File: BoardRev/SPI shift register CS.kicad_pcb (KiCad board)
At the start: 2 copper layers, 114.3 x 29.2 mm, 22 parts, among them J1 CONN_06, J10 CONN_07, J2 CONN_06, J3 CONN_06, J4 CONN_06, J5 CONN_06, J6 CONN_06, J7 CONN_06, J8 CONN_06, J9 CONN_07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

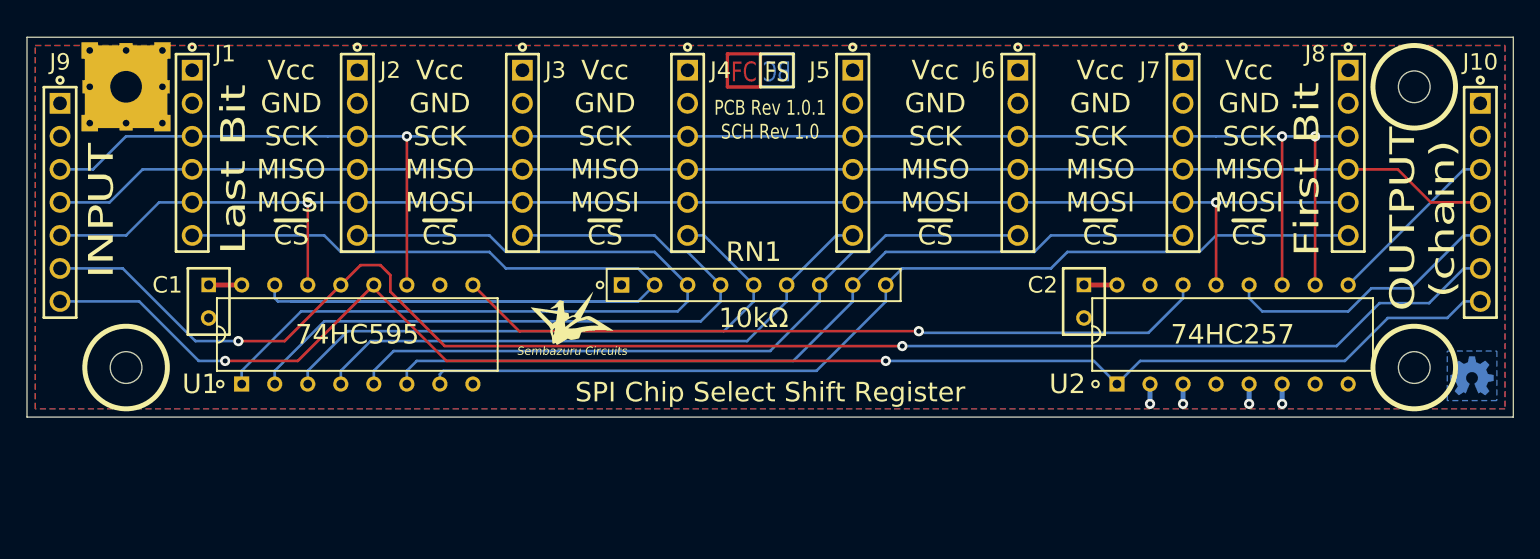
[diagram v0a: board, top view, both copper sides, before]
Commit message: Initial 1" square SMT version
Signed-off-by: Chris 'Sembazuru' Elliott <SembazuruCDE@GMail.com>
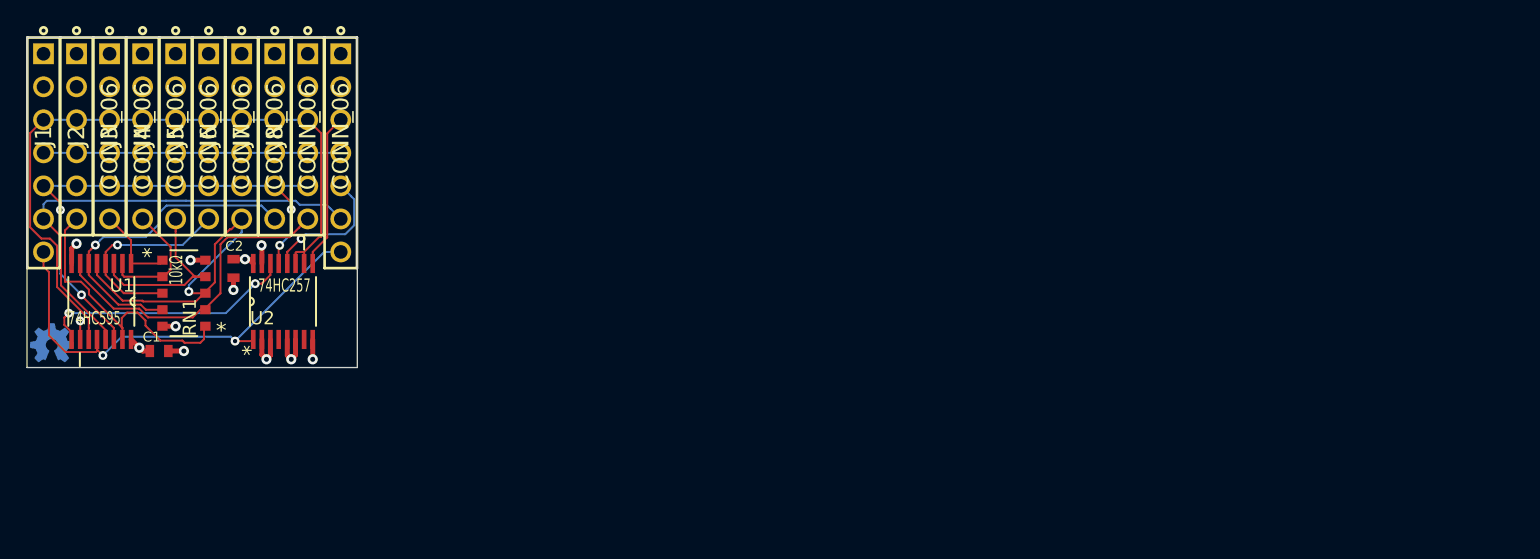
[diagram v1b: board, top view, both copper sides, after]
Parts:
- removed LayerIcon02: VAL**, Misc Unsorted New:LayerIcon02
- removed MH1: #2 Free Fit, ipc-7251TH Standard:MTGP635H244V8P
- removed MH2, MH3, MH4: #2 Free Fit, ipc-7251TH Standard:MTGNP635H244Z635P
- C1, C2: footprint ipc-7251TH Standard:CAPRR254W51L508T318H660P -> AVX-06035C104KAT2A:CAPC1608X90N
- G***: moved to B.Cu
- J1, J2, J3, J4, J5, J6, J7, J8: footprint ipc-7251TH Standard:HDRV6W64P254_1X6_1524X254X1016P -> ipc-7251TH-standard:HDRV6W64P254_1X6_1524X254X1016P
- RN1: footprint ipc-7251TH Standard:SIP249W55P254L2261H495Q9C -> CDE_misc:RESCAV_EXBA-10N
- U1: footprint ipc-7251TH Standard:DIP762W52P254L2159H381Q16C -> NXP-74HC595PW_118:SOP65P640X110-16N
- U2: footprint ipc-7251TH Standard:DIP762W52P254L2159H381Q16C -> TI-SN74HC257PW:SOP65P640X120-16N
- moved G*** 109.2 mm to (78.1, 99.7)
- moved J10 87.7 mm to (100.3, 85.1)
- moved J8 80.0 mm to (97.8, 83.8)
- moved U2 73.1 mm to (95.9, 96.5)
- moved J7 69.9 mm to (95.2, 83.8)
- moved C2 65.5 mm to (92.1, 94.0)
- moved J6 59.7 mm to (92.7, 83.8)
- moved J5 49.5 mm to (90.2, 83.8)
- moved RN1 43.8 mm to (88.3, 95.9), turned to 180 degrees
- moved J4 39.4 mm to (87.6, 83.8)
- moved J3 29.2 mm to (85.1, 83.8)
- moved G*** 21.6 mm to (96.5, 98.4), turned to 180 degrees
- moved U1 19.8 mm to (81.9, 96.5), turned to 270 degrees
- moved J2 19.1 mm to (82.5, 83.8)
- moved J1 8.98 mm to (80.0, 83.8)
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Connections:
- RN1 pad 1: VCC -> /~CS1
- RN1 pad 2: /~CS1 -> /~CS8
- RN1 pad 3: /~CS2 -> /~CS6
- RN1 pad 4: /~CS3 -> /~CS4
- RN1 pad 5: /~CS4 -> VCC
- RN1 pad 6: /~CS5 -> /~CS2
- RN1 pad 7: /~CS6 -> /~CS3
- RN1 pad 8: /~CS7 -> /~CS5
- RN1 pad 9: /~CS8 -> /~CS7
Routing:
- net /MISO: track 111.3 -> 22.9 mm
- net /~dCS: track 119.7 -> 35.9 mm, vias 2 -> 0
- net /~rCS: track 119.5 -> 36.5 mm
- net /SCK: track 134.4 -> 53.5 mm, vias 3 -> 0
- net /~CS1: track 94.7 -> 21.8 mm
- net /MOSI: track 112.8 -> 41.3 mm, vias 2 -> 4
- net /~CS2: track 65.8 -> 6.73 mm
- net /~CS8: track 75.8 -> 25.1 mm
- net /~CS3: track 55.6 -> 9.67 mm
- net /~CS7: track 65.8 -> 25.4 mm, vias 0 -> 1
- net /SerChain: track 58.3 -> 20.0 mm, vias 1 -> 2
- net /~CS4: track 45.4 -> 14.2 mm
- net /~CS6: track 55.6 -> 25.7 mm, vias 0 -> 1
- net /~CS5: track 45.4 -> 15.8 mm, vias 0 -> 1
- net /MOSI/Ser: track 21.6 -> 10.3 mm, vias 0 -> 1
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- added copper zone on In1.Cu, net GND
- added copper zone on In2.Cu, net VCC
- removed copper zone on F.Cu, net GND
- removed copper zone on B.Cu, net VCC
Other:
- board size 114.3 x 29.2 mm -> 25.4 x 25.4 mm
- copper layers 2 -> 4
- net class Default: clearance 0.2032 -> 0.1524; trace_width 0.2032 -> 0.1524; via_dia 0.7874 -> 0.6858; via_drill 0.381 -> 0.3302
- net class Power1A: clearance 0.254 -> 0.1524
- net class Power2A: clearance 0.254 -> 0.1524
- net class Power3A: clearance 0.254 -> 0.1524
- net class Power4A: clearance 0.254 -> 0.1524
- net class Power5A: clearance 0.254 -> 0.1524
- rule trace_clearance: 0.2032 -> 0.1524
- rule trace_min: 0.2032 -> 0.1524
- rule via_min_drill: 0.381 -> 0.3302
- rule via_min_size: 0.7874 -> 0.6858
- board text added: "PCB Rev 2.0.0 SCH Rev 2.0.0"
- board text added: "~dCS"
- board text added: "~rCS"
- board text removed: "First Bit"
- board text removed: "Last Bit"
- board text removed: "PCB Rev 1.0.1 SCH Rev 1.0"
- board text removed: "~CS"

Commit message: PCB v2.0.1 - Tweak routing, and push back slikscreen up 25mil to avoid vias. Ordered first batch (12pcs) from OSHPark.
Signed-off-by: Chris 'Sembazuru' Elliott <SembazuruCDE@GMail.com>
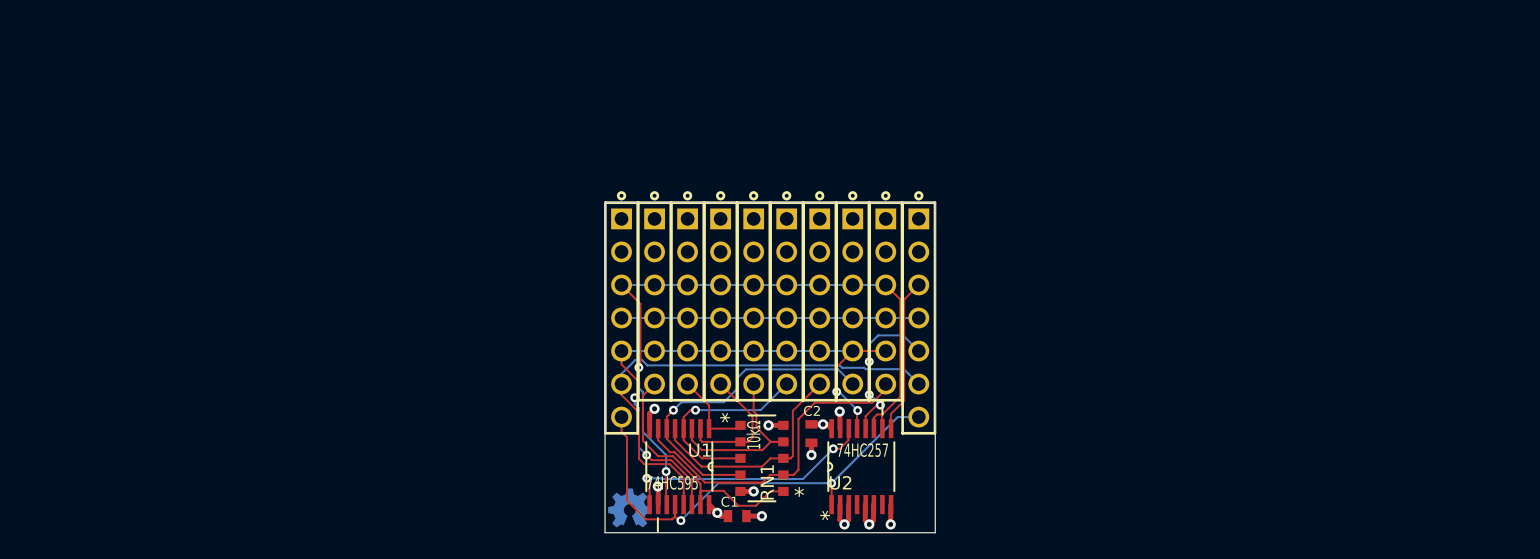
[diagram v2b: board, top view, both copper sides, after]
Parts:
- moved U2 46.3 mm to (140.4, 109.2)
- moved J4 46.2 mm to (132.1, 96.5)
- moved C1 46.2 mm to (130.8, 113.0)
- moved C2 46.2 mm to (136.5, 106.7)
- moved G*** 46.2 mm to (122.6, 112.4)
- moved J10 46.2 mm to (144.8, 97.8)
- moved J2 46.2 mm to (127.0, 96.5)
- moved J5 46.2 mm to (134.6, 96.5)
- moved J6 46.2 mm to (137.2, 96.5)
- moved J8 46.2 mm to (142.2, 96.5)
- moved J9 46.2 mm to (121.9, 97.8)
- moved RN1 46.2 mm to (132.7, 108.6)
- moved J1 46.2 mm to (124.5, 96.5)
- moved J3 46.2 mm to (129.5, 96.5)
- moved J7 46.2 mm to (139.7, 96.5)
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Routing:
- net /~CS6: track 25.7 -> 17.5 mm, vias 1 -> 0
- net /~CS1: track 21.8 -> 19.5 mm
- net /MOSI/Ser: track 10.3 -> 12.1 mm, vias 1 -> 3
- net /MOSI: track 41.3 -> 42.8 mm
- net /~dCS: track 35.9 -> 37.2 mm
- net /SCK: track 53.5 -> 52.6 mm, vias 0 -> 2
- net /~CS3: track 9.67 -> 10.2 mm
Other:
- board text added: "PCB Rev 2.0.1 SCH Rev 2.0.0"
- board text removed: "PCB Rev 2.0.0 SCH Rev 2.0.0"
